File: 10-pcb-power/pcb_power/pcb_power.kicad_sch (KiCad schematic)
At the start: 8 parts, among them J1 Pwr_jmp, U1 RP402N331F

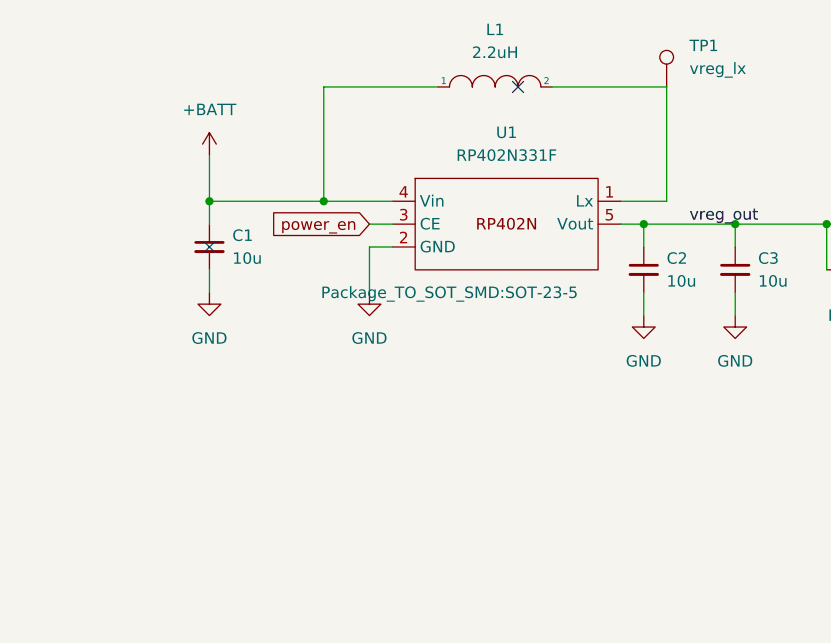
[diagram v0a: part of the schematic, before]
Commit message: more work on pwr circuitry schematic
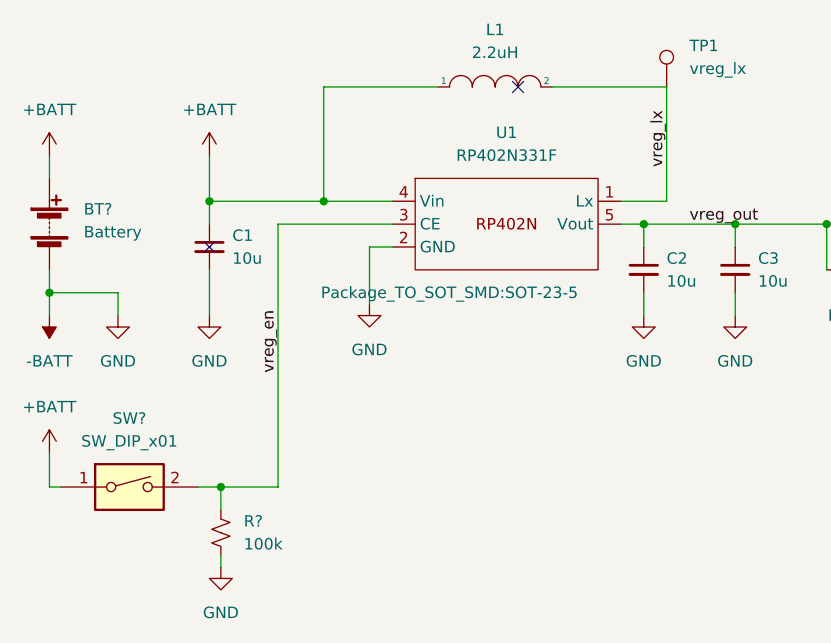
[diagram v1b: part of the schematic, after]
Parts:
- added BT?: Battery, Battery:BatteryHolder_TruPower_BH-331P_3xAA, symbol Device:Battery
- added R?: 100k, Resistor_SMD:R_0805_2012Metric, symbol Device:R_Small_US
- added SW?: SW_DIP_x01, symbol Switch:SW_DIP_x01
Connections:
- net +BATT: now also BT?.1 (+), SW?.1
- net vreg_lx: now reaches L1.2, TP1.1, U1.1 (Lx)
- net GND renamed -BATT
- net -BATT: now also BT?.2 (-), R?.2
- net power_en renamed vreg_en
- net vreg_en: now also R?.1, SW?.2

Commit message: Power Layout
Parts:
- removed R?: 100k, Resistor_SMD:R_0805_2012Metric, symbol Device:R_Small_US
- removed SW?: SW_DIP_x01, symbol Switch:SW_DIP_x01
- added SW1: SW_SPDT, Button_Switch_SMD:SW_SPDT_CK-JS102011SAQN, symbol Switch:SW_SPDT
- gave numbers to parts that had none: 1
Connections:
- net +BATT: now also SW1.3 (C)
- net vreg_en: now also SW1.2 (B)
- net -BATT renamed GND
- net GND: now also SW1.1 (A)
- no-connect marks 3 -> 0

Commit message: More PCB Work
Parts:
- added AE1: Antenna_Shield, symbol Device:Antenna_Shield
- added C4: C_Small, Capacitor_SMD:C_0805_2012Metric, symbol Device:C_Small
- added D1: LED, LED_SMD:LED_0805_2012Metric, symbol Device:LED
- added J2: CPU_jmp, Connector_PinHeader_2.54mm:PinHeader_1x02_P2.54mm_Vertical, symbol Connector:Conn_01x02_Male
- added J3: Serial Header, Connector_PinHeader_2.54mm:PinHeader_1x04_P2.54mm_Vertical, symbol Connector:Conn_01x04_Male
- added J4: Programming Header, Connector_PinHeader_2.54mm:PinHeader_1x04_P2.54mm_Vertical, symbol Connector:Conn_01x04_Male
- added JP2: CPU_jmp, Jumper:SolderJumper-2_P1.3mm_Open_TrianglePad1.0x1.5mm, symbol Jumper:SolderJumper_2_Open
- added R1, R2, R3, R4: R_Small_US, Resistor_SMD:R_0805_2012Metric, symbol Device:R_Small_US
- added SW2, SW3, SW4: SW_SPST, Button_Switch_SMD:SW_SPST_CK_RS282G05A3, symbol Switch:SW_SPST
- added U2: LoRa-E5, LoRa-E5:LoRa-E5, symbol LoRa-E5:LoRa-E5
- added U3: IN-S128TATRGB, RGB_LED:IN-S128TATRGB, symbol LED_lib:IN-S128TATRGB
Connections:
- net +3V3: now also J2.2 (Pin_2), J3.4 (Pin_4), J4.1 (Pin_1), JP2.1 (A), U3.1 (A)
- net GND: now also AE1.2 (Shield), C4.2, D1.1 (K), J3.1 (Pin_1), J4.2 (Pin_2), SW2.2 (B), SW3.2 (B), SW4.2 (B), U2.14 (GND), U2.16 (GND), U2.2 (GND), U2.22 (GND)
- new net: D1.2 (A), R4.2
- new net: R3.2, U3.2 (BK)
- new net: R1.2, U3.3 (RK)
- new net: R2.2, U3.4 (GK)
- new net BOOT/PB13: SW3.1 (A), U2.24 (PB13~{})
- new net LED_B: R3.1, U2.25 (PB9)
- new net LED_G: R2.1, U2.26 (PB14)
- new net LED_R: R1.1, U2.27 (PA10)
- new net LED_STATUS: R4.1, U2.11 (PB5)
- new net PA0/BUTTON: SW4.1 (A), U2.23 (PA0)
- new net PA15/SDA: U2.6 (PA15)
- new net PB15/SCL: U2.5 (PB15)
- new net RFIO: AE1.1 (A), U2.15 (RFIO)
- new net RST: SW2.1 (A), U2.17 (RST)
- new net RX/PB7: J3.3 (Pin_3), U2.9 (PB7)
- new net SWCLK/PA14: J4.4 (Pin_4), U2.4 (PA14)
- new net SWDIO/PA13: J4.3 (Pin_3), U2.3 (PA13)
- new net TX/PB6: J3.2 (Pin_2), U2.10 (PB6)
- new net Vcc: C4.1, J2.1 (Pin_1), JP2.2 (B), U2.1 (VCC)
- no-connect marks 0 -> 10
